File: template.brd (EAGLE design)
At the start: 124.5 x 55.9 mm, 61 parts, among them J1 RJ45KEYSTONE-942, J2 JTAG_ARM_10PIN, J3 APP_2POS_CONFIG12V_HORIZ, U1 TM4C1294NCPDT, U2 HX1198FNL, U3 SLVU2.8-4, U4 OKI-78SR-5/1.5-W36HC, U5 TPS73733DCQ, Y1 NX3225GA, Y2 CRYATL_32K_SMD

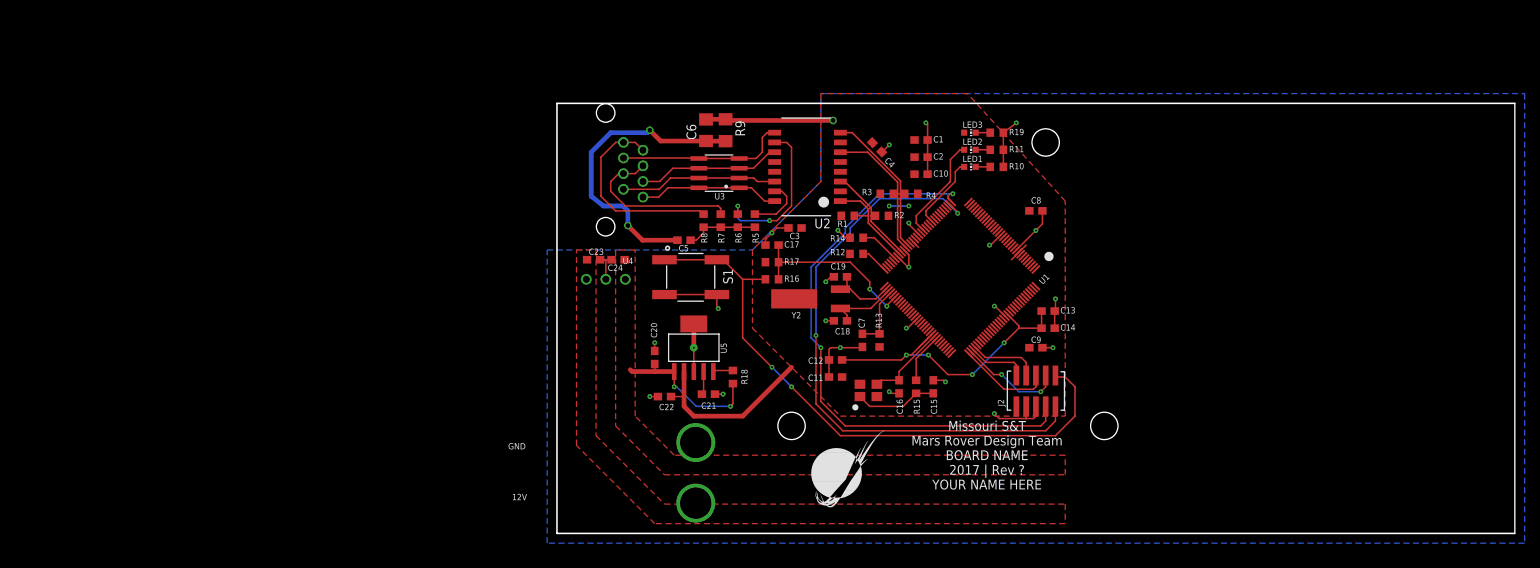
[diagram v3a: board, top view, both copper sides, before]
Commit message: Updated to match ordered Ext Controls board
Made Vias Smaller
Moved Ethernet Circuitry lower
Added Actuation Bus
Updated Libraries
Rounded Board Corners
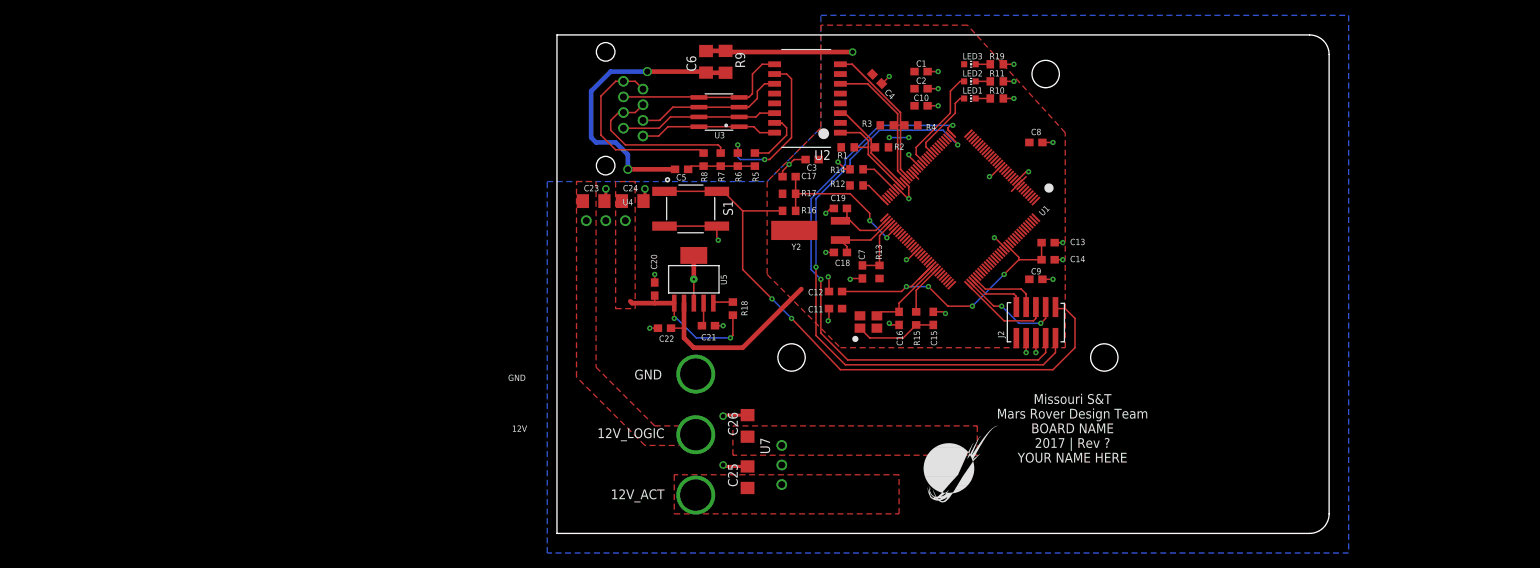
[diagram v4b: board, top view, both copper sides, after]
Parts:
- added C25, C26: 10uF, resistor:C1206
- added J8: APPPP45_PCB_HORIZ_RIGHT, MRDT-Connectors:APP45_PCB_HORIZ_RIGHT
- added U7: OKI-78SR-5/1.5-W36HC, MRDT-ICs:OKI-78SR_HORIZ
- C23, C24: device resistor:C0603 -> resistor:C1206
- moved U$1 14.6 mm to (47.6, 3.17)
- moved C5 9.21 mm to (16.2, 47.3)
- moved C3 9.16 mm to (33.2, 48.6)
- moved R17 9.16 mm to (30.2, 44.1)
- moved C17 9.16 mm to (30.2, 46.4)
- moved R16 9.16 mm to (30.2, 41.9)
- moved C18 8.89 mm to (36.8, 36.5)
- moved C9 8.89 mm to (62.2, 33.0)
- moved U5 8.89 mm to (17.8, 33.0)
- moved C1 8.89 mm to (47.3, 60.0)
- moved C10 8.89 mm to (47.3, 55.6)
- moved C11 8.89 mm to (36.2, 29.2)
- moved C12 8.89 mm to (36.2, 31.4)
- moved C13 8.89 mm to (63.8, 37.8)
- moved C14 8.89 mm to (63.8, 35.6)
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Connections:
- net +12V renamed +12V_LOGIC
- net +5V renamed +5V_LOGIC
- removed net PA2: U1.P$35
- removed net PA3: U1.P$36
- removed net PA4: U1.P$37
- removed net PA5: U1.P$38
- removed net PA6: U1.P$40
- removed net PA7: U1.P$41
- removed net PB0: U1.P$95
- removed net PB1: U1.P$96
- removed net PB2: U1.P$91
- removed net PB3: U1.P$92
- removed net PB4: U1.P$121
- removed net PB5: U1.P$120
- removed net PC4: U1.P$25
- removed net PC5: U1.P$24
- removed net PC6: U1.P$23
- removed net PC7: U1.P$22
- removed net PD0: U1.P$1
- removed net PD1: U1.P$2
- removed net PD2: U1.P$3
- removed net PD3: U1.P$4
- removed net PD4: U1.P$125
- removed net PD5: U1.P$126
- removed net PD6: U1.P$127
- removed net PD7: U1.P$128
- removed net PE0: U1.P$15
- removed net PE1: U1.P$14
- removed net PE2: U1.P$13
- removed net PE3: U1.P$12
- removed net PE4: U1.P$123
- removed net PE5: U1.P$124
- removed net PF1: U1.P$43
- removed net PF2: U1.P$44
- removed net PF3: U1.P$45
- removed net PG0: U1.P$49
- removed net PG1: U1.P$50
- removed net PH0: U1.P$29
- removed net PH1: U1.P$30
- removed net PH2: U1.P$31
- removed net PH3: U1.P$32
- removed net PJ0: U1.P$116
- removed net PJ1: U1.P$117
- removed net PK0: U1.P$18
- removed net PK1: U1.P$19
- removed net PK2: U1.P$20
- removed net PK3: U1.P$21
- removed net PK4: U1.P$63
- removed net PK5: U1.P$62
- removed net PK6: U1.P$61
- removed net PK7: U1.P$60
- removed net PL0: U1.P$81
- removed net PL1: U1.P$82
- removed net PL2: U1.P$83
- removed net PL3: U1.P$84
- removed net PL4: U1.P$85
- removed net PL5: U1.P$86
- removed net PL6: U1.P$94
- removed net PL7: U1.P$93
- removed net PM0: U1.P$78
- removed net PM1: U1.P$77
- removed net PM2: U1.P$76
- removed net PM3: U1.P$75
- removed net PM4: U1.P$74
- removed net PM5: U1.P$73
- removed net PM6: U1.P$72
- removed net PM7: U1.P$71
- removed net PN0: U1.P$107
- removed net PN1: U1.P$108
- removed net PN2: U1.P$109
- removed net PN3: U1.P$110
- removed net PN4: U1.P$111
- removed net PN5: U1.P$112
- removed net PP0: U1.P$118
- removed net PP1: U1.P$119
- removed net PP2: U1.P$103
- removed net PP3: U1.P$104
- removed net PP4: U1.P$105
- removed net PP5: U1.P$106
- removed net PQ0: U1.P$5
- removed net PQ1: U1.P$6
- removed net PQ2: U1.P$11
- removed net PQ3: U1.P$27
- removed net PQ4: U1.P$102
- new net +12V_ACT: C25.1, J8.P$1, U7.1
- new net +5V_ACT: C26.1, U7.3
- net GND: now also C25.2, C26.2, U7.2
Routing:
- net GND: track 107.0 -> 97.3 mm, vias 25 -> 38
- net !RESET: track 78.2 -> 80.8 mm
- net N_$20: track 23.1 -> 20.9 mm
- net +3V3: track 29.8 -> 31.6 mm
- net N_$15: track 39.6 -> 38.3 mm
- net N_$5: track 18.7 -> 19.6 mm
- net N_$7: track 22.2 -> 22.9 mm
- net N_$14: track 9.49 -> 8.85 mm
- added copper zone on layer 1, net +12V_ACT
- added copper zone on layer 1, net +5V_ACT
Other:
- board size 124.5 x 55.9 mm -> 100.3 x 64.8 mm
- board text added: "12V_ACT"
- board text added: "12V_LOGIC"
- board text added: "GND"
